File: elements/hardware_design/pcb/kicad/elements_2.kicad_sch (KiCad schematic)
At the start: 35 parts, among them IC10 STM32F405RGT6, Q1 8MHz, SW2 EVQQ2, SW3 EVQQ2, U1 WM8731CLSEFL

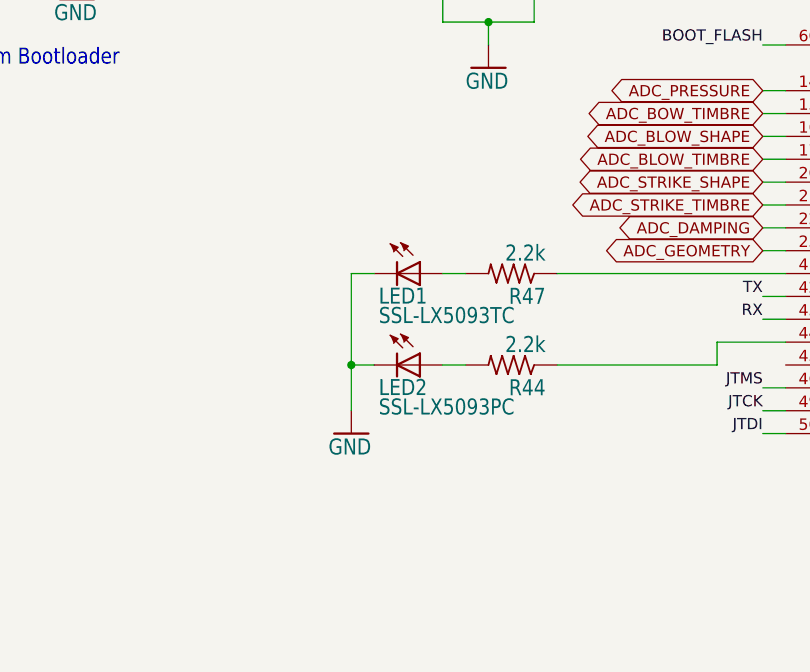
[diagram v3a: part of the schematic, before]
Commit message: SMD LEDs
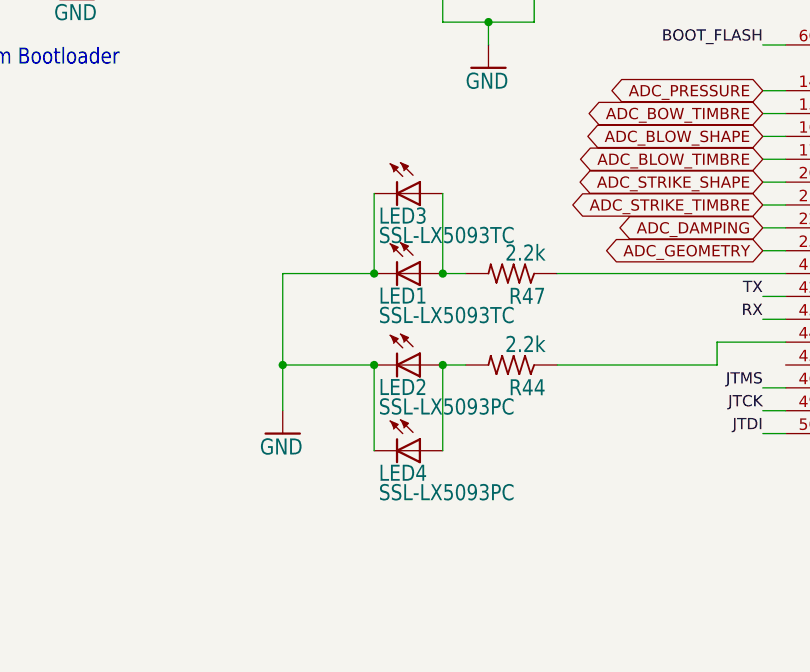
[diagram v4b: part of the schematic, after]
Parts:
- added LED3: SSL-LX5093TC, LED_SMD:LED_0603_1608Metric, symbol elements-eagle-import:LED5MM
- added LED4: SSL-LX5093PC, LED_SMD:LED_0603_1608Metric, symbol elements-eagle-import:LED5MM
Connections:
- net GND: now also LED3.K (C), LED4.K (C)
- net at LED1.A, R47.2: now also LED3.A
- net at LED2.A, R44.2: now also LED4.A
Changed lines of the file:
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@@
   (junction (at 66.04 203.2) (diameter 0) (color 0 0 0 0)
   )
-  (junction (at 88.9 144.78) (diameter 0) (color 0 0 0 0)
+  (junction (at 81.28 144.78) (diameter 0) (color 0 0 0 0)
   )
   (junction (at 371.475 184.785) (diameter 0) (color 0 0 0 0)
@@
   (junction (at 144.78 215.9) (diameter 0) (color 0 0 0 0)
   )
+  (junction (at 99.06 134.62) (diameter 0) (color 0 0 0 0)
+  )
   (junction (at 190.5 215.9) (diameter 0) (color 0 0 0 0)
   )
@@
   (junction (at 223.52 215.9) (diameter 0) (color 0 0 0 0)
   )
+  (junction (at 91.44 144.78) (diameter 0) (color 0 0 0 0)
+  )
   (junction (at 320.04 172.085) (diameter 0) (color 0 0 0 0)
   )
   (junction (at 104.14 106.68) (diameter 0) (color 0 0 0 0)
   )
+  (junction (at 99.06 144.78) (diameter 0) (color 0 0 0 0)
+  )
   (junction (at 266.7 144.78) (diameter 0) (color 0 0 0 0)
   )
@@
   (junction (at 339.725 140.335) (diameter 0) (color 0 0 0 0)
   )
+  (junction (at 91.44 134.62) (diameter 0) (color 0 0 0 0)
+  )
   (wire (pts (xy 40.64 63.5) (xy 38.1 63.5))
     (stroke (width 0) (type default) (color 0 0 0 0))
@@
     (stroke (width 0) (type default) (color 0 0 0 0))
   )
-  (wire (pts (xy 91.44 134.62) (xy 88.9 134.62))
+  (wire (pts (xy 81.28 134.62) (xy 91.44 134.62))
+    (stroke (width 0) (type default) (color 0 0 0 0))
+  )
+  (wire (pts (xy 91.44 125.73) (xy 91.44 134.62))
     (stroke (width 0) (type default) (color 0 0 0 0))
   )
@@
     (stroke (width 0) (type default) (color 0 0 0 0))
   )
-  (wire (pts (xy 88.9 134.62) (xy 88.9 144.78))
+  (wire (pts (xy 81.28 134.62) (xy 81.28 144.78))
     (stroke (width 0) (type default) (color 0 0 0 0))
   )
@@
     (stroke (width 0) (type default) (color 0 0 0 0))
   )
-  (wire (pts (xy 88.9 144.78) (xy 88.9 149.86))
+  (wire (pts (xy 81.28 144.78) (xy 81.28 149.86))
     (stroke (width 0) (type default) (color 0 0 0 0))
   )
@@
     (stroke (width 0) (type default) (color 0 0 0 0))
   )
-  (wire (pts (xy 91.44 144.78) (xy 88.9 144.78))
+  (wire (pts (xy 81.28 144.78) (xy 91.44 144.78))
     (stroke (width 0) (type default) (color 0 0 0 0))
   )
@@
     (stroke (width 0) (type default) (color 0 0 0 0))
   )
+  (wire (pts (xy 99.06 125.73) (xy 99.06 134.62))
+    (stroke (width 0) (type default) (color 0 0 0 0))
+  )
   (wire (pts (xy 137.16 114.3) (xy 134.62 114.3))
     (stroke (width 0) (type default) (color 0 0 0 0))
@@
     (stroke (width 0) (type default) (color 0 0 0 0))
   )
+  (wire (pts (xy 99.06 144.78) (xy 99.06 154.305))
+    (stroke (width 0) (type default) (color 0 0 0 0))
+  )
   (wire (pts (xy 243.84 73.66) (xy 246.38 73.66))
     (stroke (width 0) (type default) (color 0 0 0 0))
@@
   )
   (wire (pts (xy 144.78 215.9) (xy 144.78 218.44))
+    (stroke (width 0) (type default) (color 0 0 0 0))
+  )
+  (wire (pts (xy 91.44 144.78) (xy 91.44 154.305))
     (stroke (width 0) (type default) (color 0 0 0 0))
   )
@@
     (pin "2")
   )
-  (symbol (lib_id "elements-eagle-import:GND") (at 121.92 101.6 0) (unit 1)
-    (in_bom yes) (on_board yes)
-    (property "Reference" "#GND040" (id 0) (at 121.92 101.6 0)
-      (effects (font (size 1.27 1.27)) hide)
-    )
-    (property "Value" "GND" (id 1) (at 119.38 104.14 0)
-      (effects (font (size 1.778 1.5113)) (justify left bottom))
-    )
-    (property "Footprint" "elements:" (id 2) (at 121.92 101.6 0)
-      (effects (font (size 1.27 1.27)) hide)
-    )
-    (property "Datasheet" "" (id 3) (at 121.92 101.6 0)
-      (effects (font (size 1.27 1.27)) hide)
-    )
-    (pin "1")
-  )
-  (symbol (lib_id "elements-eagle-import:R-US_R0603") (at 313.055 156.845 90) (unit 1)
-    (in_bom yes) (on_board yes)
-    (property "Reference" "R53" (id 0) (at 311.5564 160.655 0)
-      (effects (font (size 1.778 1.5113)) (justify left bottom))
-    )
-    (property "Value" "2.2k" (id 1) (at 316.357 160.655 0)
-      (effects (font (size 1.778 1.5113)) (justify left bottom))
-    )
-    (property "Footprint" "elements:R0603" (id 2) (at 313.055 156.845 0)
-      (effects (font (size 1.27 1.27)) hide)
-    )
-    (property "Datasheet" "" (id 3) (at 313.055 156.845 0)
-      (effects (font (size 1.27 1.27)) hide)
-    )
-    (pin "1")
-    (pin "2")
-  )
-  (symbol (lib_id "elements-eagle-import:LED5MM") (at 96.52 134.62 270) (unit 1)
-    (in_bom yes) (on_board yes)
-    (property "Reference" "LED1" (id 0) (at 91.948 138.176 90)
-      (effects (font (size 1.778 1.5113)) (justify left bottom))
-    )
-    (property "Value" "SSL-LX5093TC" (id 1) (at 91.948 140.335 90)
-      (effects (font (size 1.778 1.5113)) (justify left bottom))
-    )
-    (property "Footprint" "elements:LED5MM" (id 2) (at 96.52 134.62 0)
-      (effects (font (size 1.27 1.27)) hide)
-    )
-    (property "Datasheet" "" (id 3) (at 96.52 134.62 0)
+  (symbol (lib_id "elements-eagle-import:LED5MM") (at 96.52 125.73 270) (unit 1)
+    (in_bom yes) (on_board yes)
+    (property "Reference" "LED3" (id 0) (at 91.948 129.286 90)
+      (effects (font (size 1.778 1.5113)) (justify left bottom))
+    )
+    (property "Value" "SSL-LX5093TC" (id 1) (at 91.948 131.445 90)
+      (effects (font (size 1.778 1.5113)) (justify left bottom))
+    )
+    (property "Footprint" "LED_SMD:LED_0603_1608Metric" (id 2) (at 96.52 125.73 0)
+      (effects (font (size 1.27 1.27)) hide)
+    )
+    (property "Datasheet" "" (id 3) (at 96.52 125.73 0)
       (effects (font (size 1.27 1.27)) hide)
     )
@@
     (pin "K")
   )
+  (symbol (lib_id "elements-eagle-import:GND") (at 121.92 101.6 0) (unit 1)
+    (in_bom yes) (on_board yes)
+    (property "Reference" "#GND040" (id 0) (at 121.92 101.6 0)
+      (effects (font (size 1.27 1.27)) hide)
+    )
+    (property "Value" "GND" (id 1) (at 119.38 104.14 0)
+      (effects (font (size 1.778 1.5113)) (justify left bottom))
+    )
+    (property "Footprint" "elements:" (id 2) (at 121.92 101.6 0)
+      (effects (font (size 1.27 1.27)) hide)
+    )
+    (property "Datasheet" "" (id 3) (at 121.92 101.6 0)
+      (effects (font (size 1.27 1.27)) hide)
+    )
+    (pin "1")
+  )
+  (symbol (lib_id "elements-eagle-import:R-US_R0603") (at 313.055 156.845 90) (unit 1)
+    (in_bom yes) (on_board yes)
+    (property "Reference" "R53" (id 0) (at 311.5564 160.655 0)
+      (effects (font (size 1.778 1.5113)) (justify left bottom))
+    )
+    (property "Value" "2.2k" (id 1) (at 316.357 160.655 0)
+      (effects (font (size 1.778 1.5113)) (justify left bottom))
+    )
+    (property "Footprint" "elements:R0603" (id 2) (at 313.055 156.845 0)
+      (effects (font (size 1.27 1.27)) hide)
+    )
+    (property "Datasheet" "" (id 3) (at 313.055 156.845 0)
+      (effects (font (size 1.27 1.27)) hide)
+    )
+    (pin "1")
+    (pin "2")
+  )
+  (symbol (lib_id "elements-eagle-import:LED5MM") (at 96.52 134.62 270) (unit 1)
+    (in_bom yes) (on_board yes)
+    (property "Reference" "LED1" (id 0) (at 91.948 138.176 90)
+      (effects (font (size 1.778 1.5113)) (justify left bottom))
+    )
+    (property "Value" "SSL-LX5093TC" (id 1) (at 91.948 140.335 90)
+      (effects (font (size 1.778 1.5113)) (justify left bottom))
+    )
+    (property "Footprint" "elements:LED5MM" (id 2) (at 96.52 134.62 0)
+      (effects (font (size 1.27 1.27)) hide)
+    )
+    (property "Datasheet" "" (id 3) (at 96.52 134.62 0)
+      (effects (font (size 1.27 1.27)) hide)
+    )
+    (pin "A")
+    (pin "K")
+  )
   (symbol (lib_id "elements-eagle-import:C-USC0603") (at 213.36 208.28 0) (unit 1)
     (in_bom yes) (on_board yes)
@@
     (pin "K")
   )
-  (symbol (lib_id "elements-eagle-import:GND") (at 88.9 152.4 0) (unit 1)
-    (in_bom yes) (on_board yes)
-    (property "Reference" "#GND0102" (id 0) (at 88.9 152.4 0)
-      (effects (font (size 1.27 1.27)) hide)
-    )
-    (property "Value" "GND" (id 1) (at 86.36 154.94 0)
-      (effects (font (size 1.778 1.5113)) (justify left bottom))
-    )
-    (property "Footprint" "elements:" (id 2) (at 88.9 152.4 0)
-      (effects (font (size 1.27 1.27)) hide)
-    )
-    (property "Datasheet" "" (id 3) (at 88.9 152.4 0)
+  (symbol (lib_id "elements-eagle-import:GND") (at 81.28 152.4 0) (unit 1)
+    (in_bom yes) (on_board yes)
+    (property "Reference" "#GND0102" (id 0) (at 81.28 152.4 0)
+      (effects (font (size 1.27 1.27)) hide)
+    )
+    (property "Value" "GND" (id 1) (at 78.74 154.94 0)
+      (effects (font (size 1.778 1.5113)) (justify left bottom))
+    )
+    (property "Footprint" "elements:" (id 2) (at 81.28 152.4 0)
+      (effects (font (size 1.27 1.27)) hide)
+    )
+    (property "Datasheet" "" (id 3) (at 81.28 152.4 0)
       (effects (font (size 1.27 1.27)) hide)
     )
@@
     (pin "2")
   )
+  (symbol (lib_id "elements-eagle-import:LED5MM") (at 96.52 154.305 270) (unit 1)
+    (in_bom yes) (on_board yes)
+    (property "Reference" "LED4" (id 0) (at 91.948 157.861 90)
+      (effects (font (size 1.778 1.5113)) (justify left bottom))
+    )
+    (property "Value" "SSL-LX5093PC" (id 1) (at 91.948 160.02 90)
+      (effects (font (size 1.778 1.5113)) (justify left bottom))
+    )
+    (property "Footprint" "LED_SMD:LED_0603_1608Metric" (id 2) (at 96.52 154.305 0)
+      (effects (font (size 1.27 1.27)) hide)
+    )
+    (property "Datasheet" "" (id 3) (at 96.52 154.305 0)
+      (effects (font (size 1.27 1.27)) hide)
+    )
+    (pin "A")
+    (pin "K")
+  )
   (symbol (lib_id "elements-eagle-import:GND") (at 381.635 200.025 0) (unit 1)
